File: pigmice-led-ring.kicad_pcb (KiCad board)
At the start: 2 copper layers, 46 x 51 mm, 57 parts, among them J1 Conn_01x02_Female, J2 Conn_01x03_Female, U1 LMR62014XMF

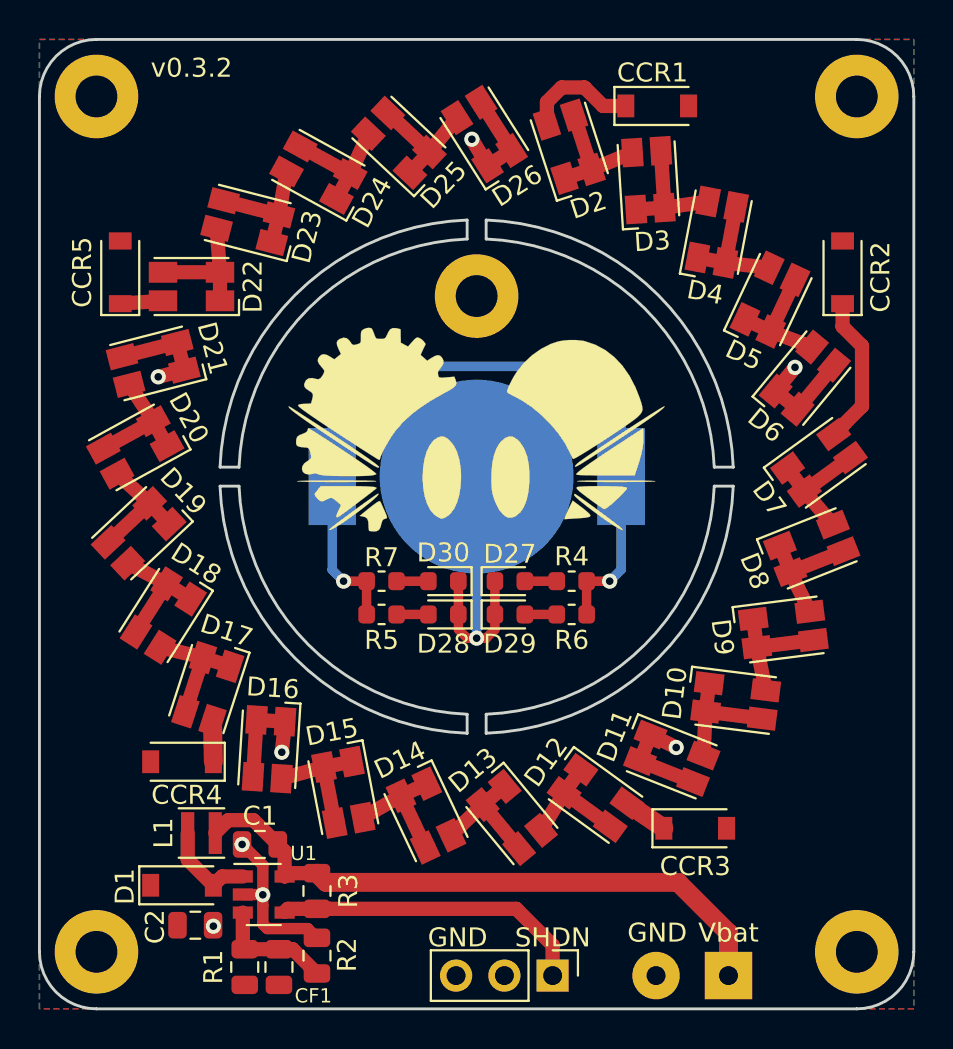
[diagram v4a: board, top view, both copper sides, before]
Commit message: Add button to mini-badge
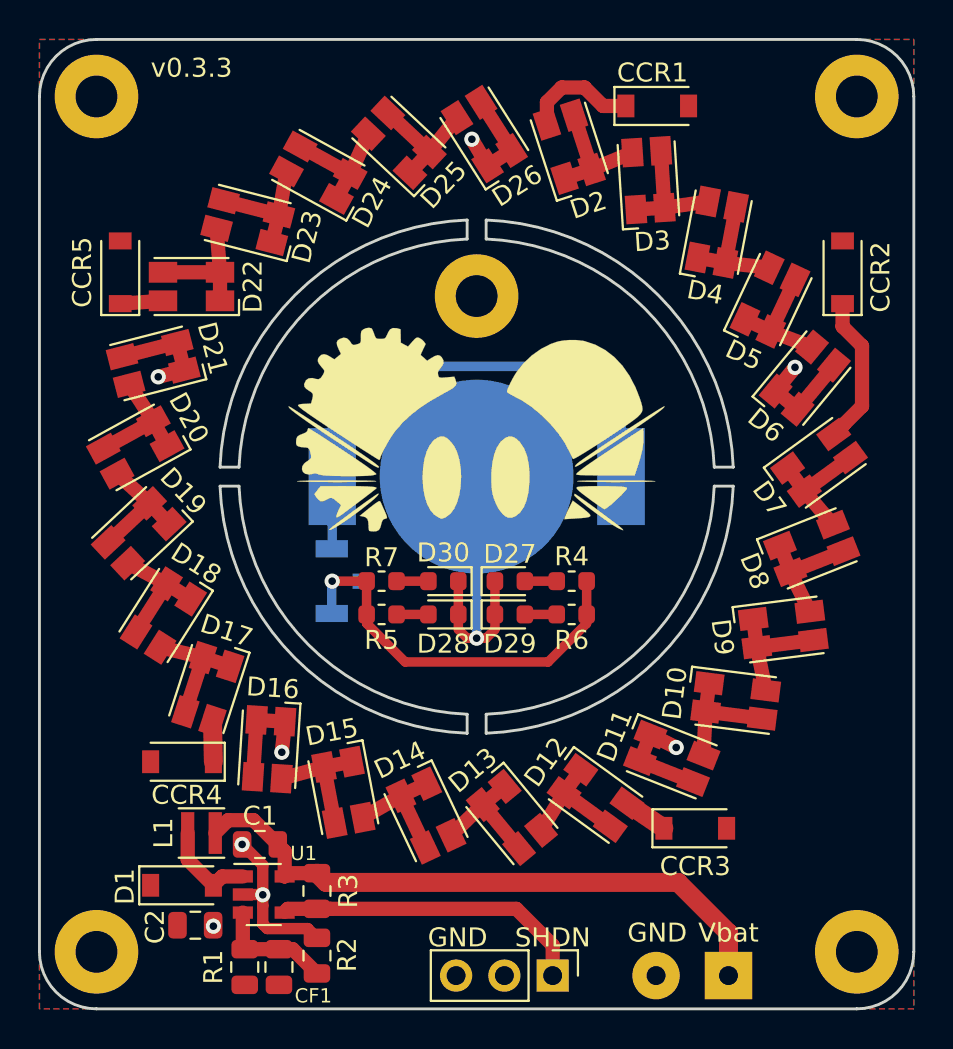
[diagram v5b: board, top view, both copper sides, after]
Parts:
- added SW1: SW_Push, Button_Switch_SMD:SW_SPST_B3U-1100P, B.Cu at (83.2, 85.5)
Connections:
- R4 pad 1: Net-(BT1-Pad1) -> Net-(R4-Pad1)
- R5 pad 1: Net-(BT1-Pad1) -> Net-(R4-Pad1)
- R6 pad 1: Net-(BT1-Pad1) -> Net-(R4-Pad1)
- R7 pad 1: Net-(BT1-Pad1) -> Net-(R4-Pad1)
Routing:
- net Net-(R4-Pad1): track 0.00 -> 21.2 mm, vias 0 -> 1
- net Net-(BT1-Pad1): track 41.0 -> 27.4 mm, vias 2 -> 0
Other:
- board text added: "v0.3.3"
- board text removed: "v0.3.2"
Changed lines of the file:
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@@
     (thickness 1.6)
     (drawings 29)
-    (tracks 164)
+    (tracks 167)
     (zones 0)
-    (modules 57)
-    (nets 38)
+    (modules 58)
+    (nets 39)
   )
   (page A4)
@@
   (net 36 "Net-(D30-Pad2)")
   (net 37 "Net-(BT1-Pad1)")
+  (net 38 "Net-(R4-Pad1)")
   (net_class Default "This is the default net class."
     (clearance 0.2)
@@
     (add_net "Net-(D7-Pad1)")
     (add_net "Net-(D8-Pad1)")
+    (add_net "Net-(R4-Pad1)")
   )
   (module MountingHole:MountingHole_2.2mm_M2_Pad (layer F.Cu)
@@
       (net 32 "Net-(D27-Pad2)"))
     (pad 1 smd roundrect (at -0.7875 0 180) (size 0.875 0.95) (layers F.Cu F.Paste F.Mask) (roundrect_rratio 0.25)
-      (net 37 "Net-(BT1-Pad1)"))
+      (net 38 "Net-(R4-Pad1)"))
     (model ${KISYS3DMOD}/Resistor_SMD.3dshapes/R_0603_1608Metric.wrl
       (at (xyz 0 0 0))
@@
       (net 34 "Net-(D28-Pad2)"))
     (pad 1 smd roundrect (at -0.7875 0) (size 0.875 0.95) (layers F.Cu F.Paste F.Mask) (roundrect_rratio 0.25)
-      (net 37 "Net-(BT1-Pad1)"))
+      (net 38 "Net-(R4-Pad1)"))
     (model ${KISYS3DMOD}/Resistor_SMD.3dshapes/R_0603_1608Metric.wrl
       (at (xyz 0 0 0))
@@
       (net 35 "Net-(D29-Pad2)"))
     (pad 1 smd roundrect (at -0.7875 0 180) (size 0.875 0.95) (layers F.Cu F.Paste F.Mask) (roundrect_rratio 0.25)
-      (net 37 "Net-(BT1-Pad1)"))
+      (net 38 "Net-(R4-Pad1)"))
     (model ${KISYS3DMOD}/Resistor_SMD.3dshapes/R_0603_1608Metric.wrl
       (at (xyz 0 0 0))
@@
       (net 36 "Net-(D30-Pad2)"))
     (pad 1 smd roundrect (at -0.7875 0) (size 0.875 0.95) (layers F.Cu F.Paste F.Mask) (roundrect_rratio 0.25)
-      (net 37 "Net-(BT1-Pad1)"))
+      (net 38 "Net-(R4-Pad1)"))
     (model ${KISYS3DMOD}/Resistor_SMD.3dshapes/R_0603_1608Metric.wrl
       (at (xyz 0 0 0))
@@
     )
   )
+  (module Button_Switch_SMD:SW_SPST_B3U-1100P (layer B.Cu)
+    (at 83.2 85.5 270)
+    (descr "Ultra-small-sized Tactile Switch with High Contact Reliability, Top-actuated Model, with Ground Terminal, without Boss")
+    (tags "Tactile Switch")
+    (attr smd)
+    (fp_text reference SW1 (at 0 3.3 270) (layer B.SilkS)
+      (effects (font (size 1 1) (thickness 0.15)) (justify mirror))
+    )
+    (fp_text value SW_Push (at 0 -2.67 270) (layer B.Fab)
+      (effects (font (size 1 1) (thickness 0.15)) (justify mirror))
+    )
+    (fp_text user %R (at 0 3.3 270) (layer B.Fab)
+      (effects (font (size 1 1) (thickness 0.15)) (justify mirror))
+    )
+    (fp_line (start -0.65 -0.82) (end -0.65 -1.63) (layer B.CrtYd) (width 0.05))
+    (fp_line (start -0.65 -1.63) (end 0.65 -1.63) (layer B.CrtYd) (width 0.05))
+    (fp_line (start 0.65 -1.63) (end 0.65 -0.82) (layer B.CrtYd) (width 0.05))
+    (fp_line (start 0.65 -0.82) (end 2.4 -0.82) (layer B.CrtYd) (width 0.05))
+    (fp_line (start -1.65 -0.57) (end -0.65 -0.57) (layer B.SilkS) (width 0.12))
+    (fp_line (start -2.4 -0.82) (end -0.65 -0.82) (layer B.CrtYd) (width 0.05))
+    (fp_line (start 2.4 -0.82) (end 2.4 2.47) (layer B.CrtYd) (width 0.05))
+    (fp_line (start 2.4 2.47) (end -2.4 2.47) (layer B.CrtYd) (width 0.05))
+    (fp_line (start -2.4 2.47) (end -2.4 -0.82) (layer B.CrtYd) (width 0.05))
+    (fp_line (start -1.65 -0.28) (end -1.65 -0.57) (layer B.SilkS) (width 0.12))
+    (fp_line (start 1.65 -0.57) (end 0.65 -0.57) (layer B.SilkS) (width 0.12))
+    (fp_line (start 1.65 -0.57) (end 1.65 -0.28) (layer B.SilkS) (width 0.12))
+    (fp_line (start -1.65 1.93) (end -1.65 2.22) (layer B.SilkS) (width 0.12))
+    (fp_line (start -1.65 2.22) (end 1.65 2.22) (layer B.SilkS) (width 0.12))
+    (fp_line (start 1.65 2.22) (end 1.65 1.93) (layer B.SilkS) (width 0.12))
+    (fp_line (start -1.5 2.08) (end 1.5 2.08) (layer B.Fab) (width 0.1))
+    (fp_line (start 1.5 2.08) (end 1.5 -0.43) (layer B.Fab) (width 0.1))
+    (fp_line (start 1.5 -0.43) (end -1.5 -0.43) (layer B.Fab) (width 0.1))
+    (fp_line (start -1.5 -0.43) (end -1.5 2.08) (layer B.Fab) (width 0.1))
+    (fp_circle (center 0 0.82) (end 0.75 0.82) (layer B.Fab) (width 0.1))
+    (pad 1 smd rect (at -1.7 0.82 270) (size 0.9 1.7) (layers B.Cu B.Paste B.Mask)
+      (net 37 "Net-(BT1-Pad1)"))
+    (pad 2 smd rect (at 1.7 0.82 270) (size 0.9 1.7) (layers B.Cu B.Paste B.Mask)
+      (net 38 "Net-(R4-Pad1)"))
+    (pad 3 smd rect (at 0 -0.82 270) (size 0.8 1.1) (layers B.Cu B.Paste B.Mask))
+    (model ${KISYS3DMOD}/Button_Switch_SMD.3dshapes/SW_SPST_B3U-1100P.wrl
+      (at (xyz 0 0 0))
+      (scale (xyz 1 1 1))
+      (rotate (xyz 0 0 0))
+    )
+  )
   (gr_line (start 103.499999 80.500001) (end 102.499999 80.500001) (layer Edge.Cuts) (width 0.15))
   (gr_line (start 102.499999 79.500001) (end 103.499999 79.500001) (layer Edge.Cuts) (width 0.15))
@@
   (gr_line (start 110 57) (end 70 57) (layer Edge.Cuts) (width 0.15))
   (gr_line (start 70 108) (end 110 108) (layer Edge.Cuts) (width 0.15))
-  (gr_text v0.3.2 (at 75 58.5) (layer F.SilkS)
+  (gr_text v0.3.3 (at 75 58.5) (layer F.SilkS)
     (effects (font (size 1 1) (thickness 0.15)))
   )
@@
   (segment (start 90.9625 85.5) (end 90.9625 87.25) (width 0.5) (layer F.Cu) (net 33) (status 30))
   (via (at 90 88.5) (size 0.8) (drill 0.4) (layers F.Cu B.Cu) (net 33))
-  (segment (start 90 80) (end 90 88.5) (width 0.5) (layer B.Cu) (net 33))
+  (segment (start 90 80) (end 90 88.5) (width 0.5) (layer B.Cu) (net 33) (status 10))
   (segment (start 90 88.5) (end 89.5 88.5) (width 0.5) (layer F.Cu) (net 33))
-  (segment (start 89.0375 88.0375) (end 89.0375 87.25) (width 0.5) (layer F.Cu) (net 33))
+  (segment (start 89.0375 88.0375) (end 89.0375 87.25) (width 0.5) (layer F.Cu) (net 33) (status 20))
   (segment (start 89.5 88.5) (end 89.0375 88.0375) (width 0.5) (layer F.Cu) (net 33))
   (segment (start 90 88.5) (end 90.5 88.5) (width 0.5) (layer F.Cu) (net 33))
-  (segment (start 90.9625 88.0375) (end 90.9625 87.25) (width 0.5) (layer F.Cu) (net 33))
+  (segment (start 90.9625 88.0375) (end 90.9625 87.25) (width 0.5) (layer F.Cu) (net 33) (status 20))
   (segment (start 90.5 88.5) (end 90.9625 88.0375) (width 0.5) (layer F.Cu) (net 33))
   (segment (start 87.4625 87.25) (end 85.7875 87.25) (width 0.5) (layer F.Cu) (net 34) (status 30))
   (segment (start 94.2125 87.25) (end 92.5375 87.25) (width 0.5) (layer F.Cu) (net 35) (status 30))
   (segment (start 85.7875 85.5) (end 87.4625 85.5) (width 0.5) (layer F.Cu) (net 36) (status 30))
-  (segment (start 95.7875 85.5) (end 95.7875 87.25) (width 0.5) (layer F.Cu) (net 37) (status 30))
-  (segment (start 84.2125 85.5) (end 84.2125 87.25) (width 0.5) (layer F.Cu) (net 37) (status 30))
-  (via (at 83 85.5) (size 0.8) (drill 0.4) (layers F.Cu B.Cu) (net 37))
-  (segment (start 82.4 80) (end 82.4 84.9) (width 0.5) (layer B.Cu) (net 37))
-  (segment (start 82.4 84.9) (end 83 85.5) (width 0.5) (layer B.Cu) (net 37))
-  (segment (start 83 85.5) (end 84.2125 85.5) (width 0.5) (layer F.Cu) (net 37))
-  (via (at 97 85.5) (size 0.8) (drill 0.4) (layers F.Cu B.Cu) (net 37))
-  (segment (start 97.6 80) (end 97.6 84.9) (width 0.5) (layer B.Cu) (net 37))
-  (segment (start 97.6 84.9) (end 97 85.5) (width 0.5) (layer B.Cu) (net 37))
-  (segment (start 97 85.5) (end 95.7875 85.5) (width 0.5) (layer F.Cu) (net 37))
   (segment (start 82.4 76.95) (end 85.15 74.2) (width 0.5) (layer B.Cu) (net 37))
-  (segment (start 82.4 80) (end 82.4 76.95) (width 0.5) (layer B.Cu) (net 37))
-  (segment (start 97.6 76.95) (end 97.6 80) (width 0.5) (layer B.Cu) (net 37))
+  (segment (start 82.4 80) (end 82.4 76.95) (width 0.5) (layer B.Cu) (net 37) (status 10))
+  (segment (start 97.6 76.95) (end 97.6 80) (width 0.5) (layer B.Cu) (net 37) (status 20))
   (segment (start 94.85 74.2) (end 97.6 76.95) (width 0.5) (layer B.Cu) (net 37))
+  (segment (start 82.4 83.78) (end 82.38 83.8) (width 0.5) (layer B.Cu) (net 37))
+  (segment (start 82.4 80) (end 82.4 83.78) (width 0.5) (layer B.Cu) (net 37))
   (segment (start 85.15 74.2) (end 94.85 74.2) (width 0.5) (layer B.Cu) (net 37))
+  (via (at 82.4 85.5) (size 0.8) (drill 0.4) (layers F.Cu B.Cu) (net 38))
+  (segment (start 82.38 87.2) (end 82.38 85.52) (width 0.5) (layer B.Cu) (net 38))
+  (segment (start 82.38 85.52) (end 82.4 85.5) (width 0.5) (layer B.Cu) (net 38))
+  (segment (start 82.4 85.5) (end 84.2125 85.5) (width 0.5) (layer F.Cu) (net 38))
+  (segment (start 84.2125 85.5) (end 84.2125 87.25) (width 0.5) (layer F.Cu) (net 38))
+  (segment (start 95.7875 85.5) (end 95.7875 87.25) (width 0.5) (layer F.Cu) (net 38))
+  (segment (start 93.7625 89.75) (end 95.7875 87.725) (width 0.5) (layer F.Cu) (net 38))
+  (segment (start 86.2375 89.75) (end 93.7625 89.75) (width 0.5) (layer F.Cu) (net 38))
+  (segment (start 84.2125 87.725) (end 86.2375 89.75) (width 0.5) (layer F.Cu) (net 38))
+  (segment (start 95.7875 87.725) (end 95.7875 87.25) (width 0.5) (layer F.Cu) (net 38))
+  (segment (start 84.2125 87.25) (end 84.2125 87.725) (width 0.5) (layer F.Cu) (net 38))
   (zone (net 1) (net_name GND) (layer B.Cu) (hatch edge 0.508)
     (connect_pads (clearance 0.508))

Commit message: Move SHDN and Vbat traces a bit
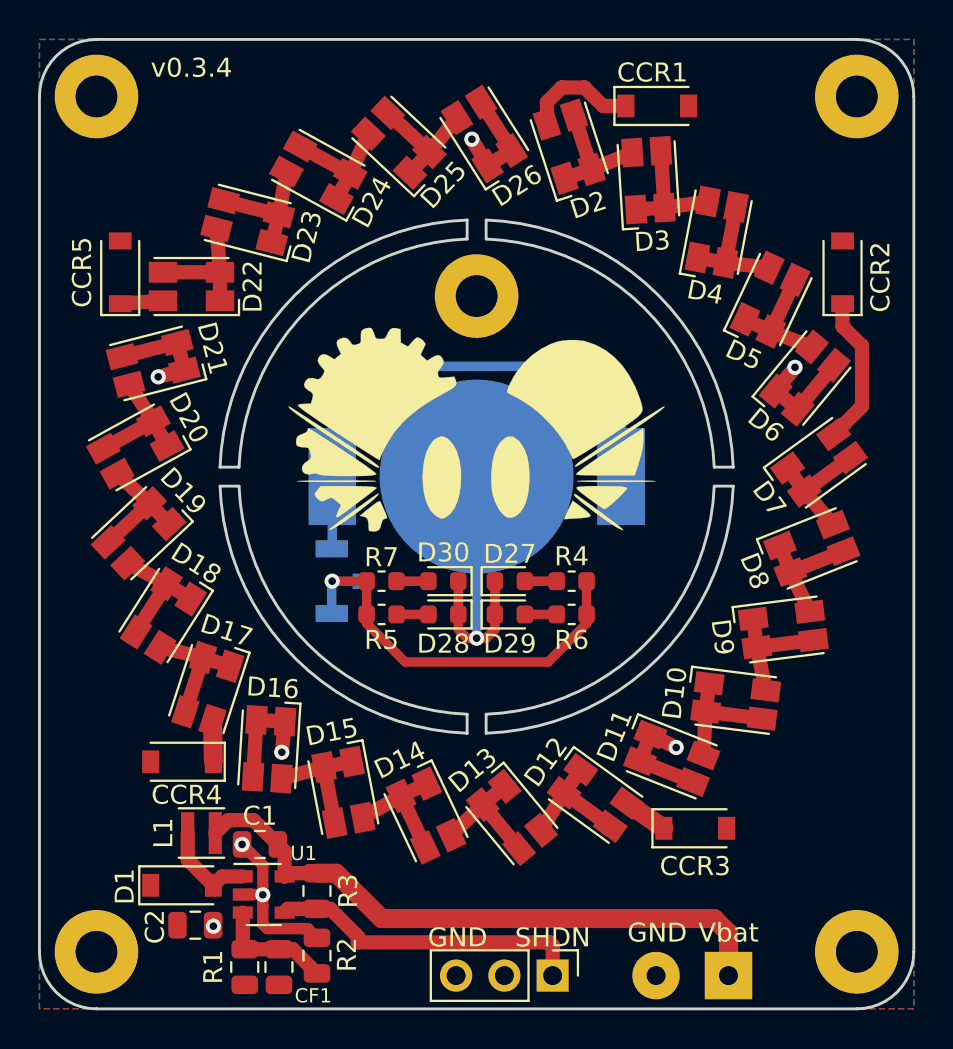
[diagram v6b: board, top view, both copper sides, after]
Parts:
- moved G*** 0.39 mm to (109.5, 96.5)
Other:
- board text added: "v0.3.4"
- board text removed: "v0.3.3"
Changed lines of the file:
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@@
     (thickness 1.6)
     (drawings 29)
-    (tracks 167)
+    (tracks 170)
     (zones 0)
     (modules 58)
@@
   )
   (setup
-    (last_trace_width 0.5)
+    (last_trace_width 1)
     (user_trace_width 0.5)
     (user_trace_width 0.6)
@@
   )
   (module led-ring:logo (layer F.Cu)
-    (at 109.22 96.774 90)
+    (at 109.5 96.5 90)
     (fp_text reference G*** (at 0 0 90) (layer F.Mask) hide
       (effects (font (size 1.524 1.524) (thickness 0.3)))
@@
   (gr_line (start 110 57) (end 70 57) (layer Edge.Cuts) (width 0.15))
   (gr_line (start 70 108) (end 110 108) (layer Edge.Cuts) (width 0.15))
-  (gr_text v0.3.3 (at 75 58.5) (layer F.SilkS)
+  (gr_text v0.3.4 (at 75 58.5) (layer F.SilkS)
     (effects (font (size 1 1) (thickness 0.15)))
   )
@@
   (segment (start 78.26249 98.07499) (end 76.92501 98.07499) (width 0.75) (layer F.Cu) (net 6))
   (segment (start 79.5375 99.35) (end 78.26249 98.07499) (width 0.75) (layer F.Cu) (net 6) (status 10))
-  (segment (start 100.597707 101.348027) (end 103.25 104.00032) (width 1) (layer F.Cu) (net 6))
-  (segment (start 82.085527 101.348027) (end 100.597707 101.348027) (width 1) (layer F.Cu) (net 6))
-  (segment (start 103.25 104.00032) (end 103.25 106.25) (width 1) (layer F.Cu) (net 6) (status 20))
-  (segment (start 81.6 100.8625) (end 82.085527 101.348027) (width 1) (layer F.Cu) (net 6) (status 10))
+  (segment (start 103.25 104.00032) (end 102.49968 103.25) (width 1) (layer F.Cu) (net 6))
+  (segment (start 103.25 106.25) (end 103.25 104.00032) (width 1) (layer F.Cu) (net 6))
+  (segment (start 102.49968 103.25) (end 85 103.25) (width 1) (layer F.Cu) (net 6))
+  (segment (start 82.6125 100.8625) (end 81.6 100.8625) (width 1) (layer F.Cu) (net 6))
+  (segment (start 85 103.25) (end 82.6125 100.8625) (width 1) (layer F.Cu) (net 6))
   (segment (start 99.692743 62.857561) (end 99.881114 65.851641) (width 0.75) (layer F.Cu) (net 7) (status 30))
   (segment (start 98.384075 65.945827) (end 99.881114 65.851641) (width 0.75) (layer F.Cu) (net 7) (status 30))
@@
   (segment (start 87.517805 62.922202) (end 88.968892 61.112191) (width 0.75) (layer F.Cu) (net 25) (status 30))
   (segment (start 81.402661 102.934839) (end 81.6 102.7375) (width 0.5) (layer F.Cu) (net 26) (status 30))
-  (segment (start 82.3 102.7375) (end 81.6 102.7375) (width 0.75) (layer F.Cu) (net 26) (status 20))
-  (segment (start 92.0875 102.7375) (end 82.3 102.7375) (width 0.75) (layer F.Cu) (net 26))
-  (segment (start 94 104.65) (end 92.0875 102.7375) (width 0.75) (layer F.Cu) (net 26))
-  (segment (start 94 106.25) (end 94 104.65) (width 0.75) (layer F.Cu) (net 26) (status 10))
   (segment (start 80.064463 102.7375) (end 79.9 102.901963) (width 0.75) (layer F.Cu) (net 26) (status 30))
   (segment (start 81.6 102.7375) (end 80.064463 102.7375) (width 0.75) (layer F.Cu) (net 26) (status 30))
+  (segment (start 94 104.65) (end 93.85 104.5) (width 0.75) (layer F.Cu) (net 26))
+  (segment (start 94 106.25) (end 94 104.65) (width 0.75) (layer F.Cu) (net 26))
+  (segment (start 93.85 104.5) (end 83.75 104.5) (width 0.75) (layer F.Cu) (net 26))
+  (segment (start 83.75 104.1875) (end 82.3 102.7375) (width 0.75) (layer F.Cu) (net 26))
+  (segment (start 82.3 102.7375) (end 81.6 102.7375) (width 0.75) (layer F.Cu) (net 26))
+  (segment (start 83.75 104.5) (end 83.75 104.1875) (width 0.75) (layer F.Cu) (net 26))
   (segment (start 96.65 60.5) (end 97.85 60.5) (width 0.75) (layer F.Cu) (net 27) (status 20))
   (segment (start 95.677372 59.527372) (end 96.65 60.5) (width 0.75) (layer F.Cu) (net 27))
